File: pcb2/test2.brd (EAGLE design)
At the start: 7 x 6.9 mm, 56 parts, among them IC1 LMV358M, IC2 LMV358M, IC3 STM32F10XCXT6, Q1 8mhz

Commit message: ready to facturing
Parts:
- C-ADCBATT: value (none) -> 100nf
- C-CLK1, C-CLK2: value (none) -> 22pf
- R-ADCBATT2: value 4k7 -> 1k5
- R-ADCLAMP1, R-ADCLAMP2, R-ADCLAMP3, R-ADCPV1, R-ADCPV2, R-ADCPV3, R-ADCUSB1, R-ADCUSB2, R-ADCUSB3: value 4k7 -> 100k
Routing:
- removed copper zone on layer 1, net N$19
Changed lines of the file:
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@@
 <layer number="18" name="Vias" color="2" fill="1" visible="yes" active="yes"/>
 <layer number="19" name="Unrouted" color="6" fill="1" visible="yes" active="yes"/>
-<layer number="20" name="Dimension" color="15" fill="1" visible="yes" active="yes"/>
+<layer number="20" name="Dimension" color="15" fill="1" visible="no" active="yes"/>
 <layer number="21" name="tPlace" color="7" fill="1" visible="yes" active="yes"/>
 <layer number="22" name="bPlace" color="7" fill="1" visible="yes" active="yes"/>
@@
 <text x="77.724" y="15.367" size="1.9304" layer="16" font="vector" ratio="10" rot="MR0">SYSTEM</text>
 <text x="30.861" y="47.879" size="1.9304" layer="16" font="vector" ratio="10" rot="MR0">v2.0</text>
+<wire x1="60.96" y1="45.974" x2="-0.254" y2="45.974" width="0.4064" layer="21"/>
+<wire x1="61.087" y1="47.879" x2="95.885" y2="47.879" width="0.4064" layer="21"/>
+<wire x1="99.949" y1="41.402" x2="76.962" y2="41.402" width="0.4064" layer="21"/>
+<wire x1="74.168" y1="41.529" x2="74.168" y2="31.623" width="0.4064" layer="21"/>
+<wire x1="76.2" y1="36.322" x2="76.2" y2="26.289" width="0.4064" layer="21"/>
+<wire x1="59.182" y1="31.115" x2="43.815" y2="31.115" width="0.4064" layer="21"/>
+<wire x1="39.37" y1="38.1" x2="39.37" y2="27.94" width="0.4064" layer="21"/>
+<wire x1="35.306" y1="39.37" x2="35.306" y2="32.639" width="0.4064" layer="21"/>
+<wire x1="55.499" y1="25.273" x2="22.225" y2="25.273" width="0.4064" layer="21"/>
+<wire x1="51.435" y1="23.241" x2="23.495" y2="23.241" width="0.4064" layer="21"/>
+<wire x1="20.193" y1="26.416" x2="20.193" y2="34.671" width="0.4064" layer="21"/>
+<wire x1="47.117" y1="20.701" x2="18.161" y2="20.701" width="0.4064" layer="21"/>
+<wire x1="44.577" y1="5.207" x2="44.577" y2="15.24" width="0.4064" layer="21"/>
+<wire x1="15.494" y1="23.495" x2="3.556" y2="23.495" width="0.4064" layer="21"/>
+<wire x1="15.24" y1="27.813" x2="4.572" y2="27.813" width="0.4064" layer="21"/>
+<wire x1="15.24" y1="33.02" x2="2.54" y2="33.02" width="0.4064" layer="21"/>
+<wire x1="-3.429" y1="65.024" x2="103.124" y2="65.024" width="0.4064" layer="21"/>
+<wire x1="103.124" y1="65.024" x2="103.124" y2="2.286" width="0.4064" layer="21"/>
+<wire x1="103.124" y1="2.286" x2="-3.429" y2="2.286" width="0.4064" layer="21"/>
+<wire x1="-3.429" y1="2.286" x2="-3.429" y2="65.024" width="0.4064" layer="21"/>
 </plain>
 <attributes>
@@
 <element name="C-USB2" library="resistor" package="E2,5-5" value="220uF" x="80.391" y="34.925"/>
 <element name="IC1" library="linear" package="SO08" value="LMV358M" x="25.908" y="40.386" rot="MR90"/>
-<element name="R-ADCPV2" library="resistor" package="R0805" value="4k7" x="19.812" y="39.624" rot="MR0"/>
-<element name="R-ADCPV1" library="resistor" package="R0805" value="4k7" x="17.018" y="40.513" rot="MR270"/>
-<element name="R-ADCPV3" library="resistor" package="R0805" value="4k7" x="19.812" y="37.719" rot="MR180"/>
+<element name="R-ADCPV2" library="resistor" package="R0805" value="100k" x="19.812" y="39.624" rot="MR0"/>
+<element name="R-ADCPV1" library="resistor" package="R0805" value="100k" x="17.018" y="40.513" rot="MR270"/>
+<element name="R-ADCPV3" library="resistor" package="R0805" value="100k" x="19.812" y="37.719" rot="MR180"/>
 <element name="D-PV1" library="diode" package="DO-214AC" value="" x="17.018" y="46.101" rot="MR90"/>
 <element name="IC2" library="linear" package="SO08" value="LMV358M" x="70.358" y="38.227" rot="MR90"/>
-<element name="R-ADCLAMP2" library="resistor" package="R0805" value="4k7" x="59.055" y="39.751" rot="MR180"/>
-<element name="R-ADCLAMP1" library="resistor" package="R0805" value="4k7" x="55.88" y="40.64" rot="MR90"/>
-<element name="R-ADCLAMP3" library="resistor" package="R0805" value="4k7" x="59.055" y="37.465" rot="MR0"/>
+<element name="R-ADCLAMP2" library="resistor" package="R0805" value="100k" x="59.055" y="39.751" rot="MR180"/>
+<element name="R-ADCLAMP1" library="resistor" package="R0805" value="100k" x="55.88" y="40.64" rot="MR90"/>
+<element name="R-ADCLAMP3" library="resistor" package="R0805" value="100k" x="59.055" y="37.465" rot="MR0"/>
 <element name="D-LAMP1" library="diode" package="DO-214AC" value="" x="55.88" y="46.609" rot="MR90"/>
-<element name="R-ADCUSB1" library="resistor" package="R0805" value="4k7" x="89.535" y="40.132" rot="MR90"/>
-<element name="R-ADCUSB2" library="resistor" package="R0805" value="4k7" x="92.71" y="39.37" rot="MR0"/>
-<element name="R-ADCUSB3" library="resistor" package="R0805" value="4k7" x="92.71" y="37.338" rot="MR180"/>
+<element name="R-ADCUSB1" library="resistor" package="R0805" value="100k" x="89.535" y="40.132" rot="MR90"/>
+<element name="R-ADCUSB2" library="resistor" package="R0805" value="100k" x="92.71" y="39.37" rot="MR0"/>
+<element name="R-ADCUSB3" library="resistor" package="R0805" value="100k" x="92.71" y="37.338" rot="MR180"/>
 <element name="D-USB1" library="diode" package="DO-214AC" value="" x="89.662" y="45.847" rot="MR90"/>
 <element name="LED1" library="led" package="CHIP-LED0805" value="" x="39.624" y="14.351" rot="MR90"/>
@@
 <element name="LED6" library="led" package="CHIP-LED0805" value="" x="39.624" y="24.257" rot="MR90"/>
 <element name="R-ADCBATT1" library="resistor" package="R0805" value="4k7" x="22.987" y="27.432" rot="MR180"/>
-<element name="R-ADCBATT2" library="resistor" package="R0805" value="4k7" x="26.67" y="27.432" rot="MR0"/>
-<element name="C-ADCBATT" library="resistor" package="C0805" value="" x="26.67" y="29.464" rot="MR0"/>
+<element name="R-ADCBATT2" library="resistor" package="R0805" value="1k5" x="26.67" y="27.432" rot="MR0"/>
+<element name="C-ADCBATT" library="resistor" package="C0805" value="100nf" x="26.67" y="29.464" rot="MR0"/>
 <element name="S-NRST" library="switch" package="SKHMPXE010" value="SKHMPSE010" x="11.303" y="23.749" rot="MR0"/>
 <element name="R-NRST" library="resistor" package="R0805" value="4k7" x="17.78" y="23.495" rot="MR90"/>
@@
 <attribute name="OC_FARNELL" value="1667008" x="-31.75" y="-66.929" size="1.778" layer="27" rot="R270" display="off"/>
 </element>
-<element name="C-CLK1" library="resistor" package="C0805" value="" x="14.478" y="12.192" rot="MR270"/>
-<element name="C-CLK2" library="resistor" package="C0805" value="" x="14.605" y="16.129" rot="MR90"/>
+<element name="C-CLK1" library="resistor" package="C0805" value="22pf" x="14.478" y="12.192" rot="MR270"/>
+<element name="C-CLK2" library="resistor" package="C0805" value="22pf" x="14.605" y="16.129" rot="MR90"/>
 <element name="FLASH" library="pinhead" package="1X04" value="" x="37.719" y="10.287" rot="R180"/>
 <element name="X1" library="con-berg" package="PN87520" value="" x="67.056" y="58.547" rot="R180">
@@
 <vertex x="-2.921" y="64.262"/>
 <vertex x="102.362" y="64.262"/>
-<vertex x="102.362" y="2.921"/>
-<vertex x="-2.921" y="2.921"/>
-</polygon>
-</signal>
-<signal name="N$19">
-<polygon width="0.8128" layer="1" isolate="0.8128">
-<vertex x="-2.921" y="64.262"/>
-<vertex x="102.362" y="64.262"/>

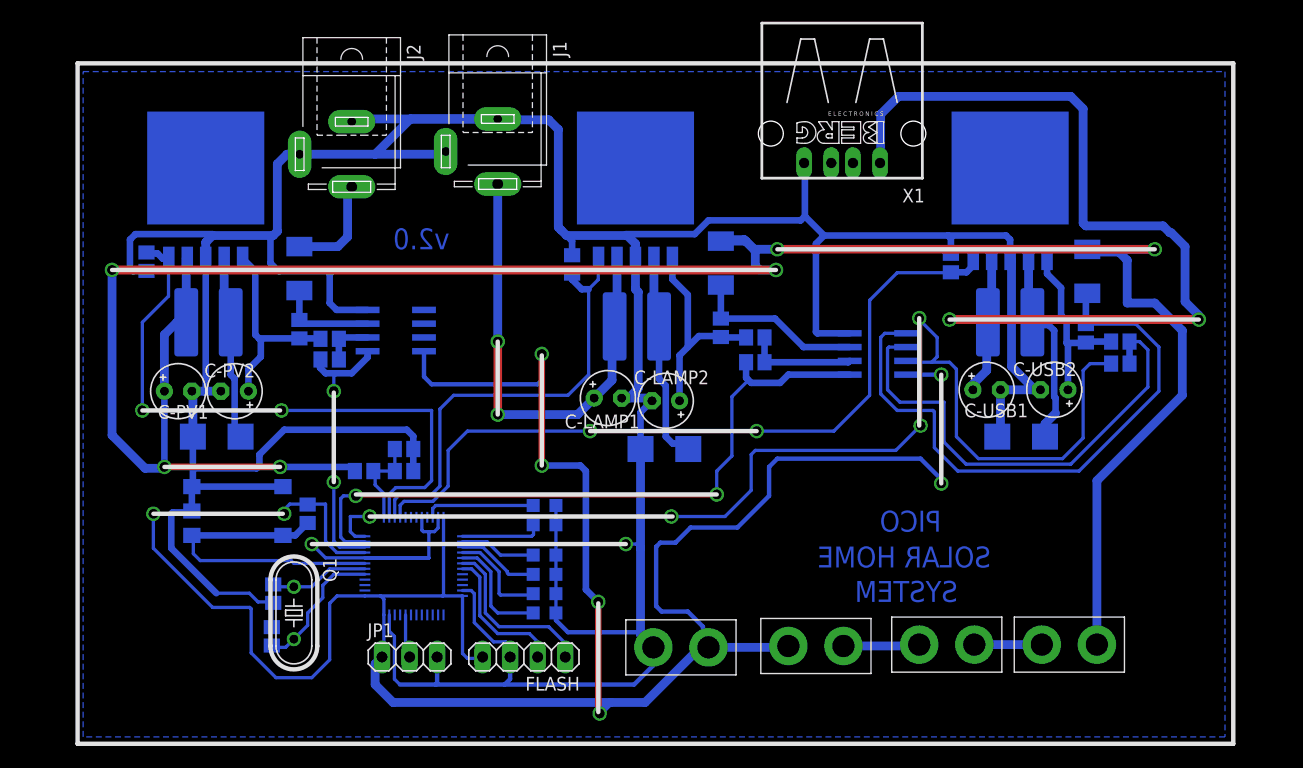
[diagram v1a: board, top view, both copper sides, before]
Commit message: add mount holes
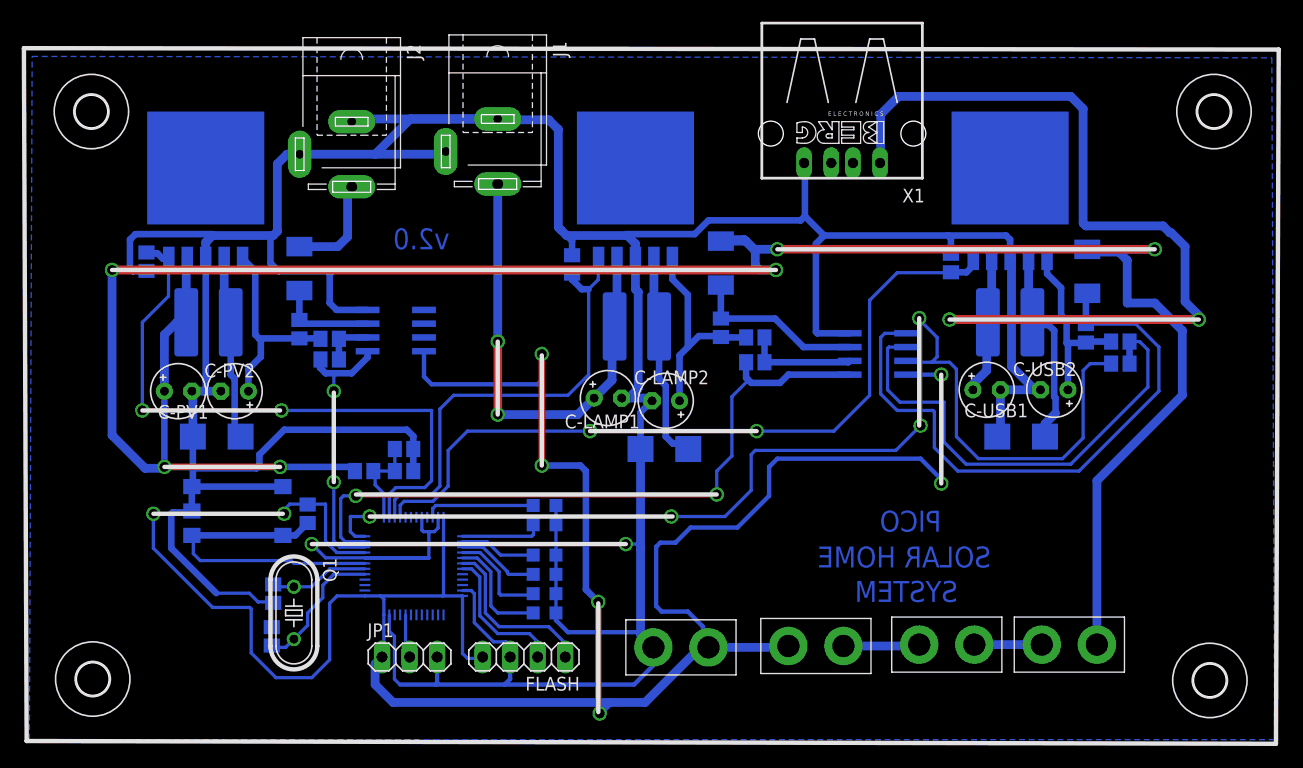
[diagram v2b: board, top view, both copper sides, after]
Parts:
- added H1, H2, H3, H4: MOUNT-HOLE3.0, holes:3,0
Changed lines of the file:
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@@
 <layer number="21" name="tPlace" color="7" fill="1" visible="yes" active="yes"/>
 <layer number="22" name="bPlace" color="7" fill="1" visible="yes" active="yes"/>
-<layer number="23" name="tOrigins" color="15" fill="1" visible="no" active="yes"/>
-<layer number="24" name="bOrigins" color="15" fill="1" visible="no" active="yes"/>
+<layer number="23" name="tOrigins" color="15" fill="1" visible="yes" active="yes"/>
+<layer number="24" name="bOrigins" color="15" fill="1" visible="yes" active="yes"/>
 <layer number="25" name="tNames" color="7" fill="1" visible="no" active="yes"/>
 <layer number="26" name="bNames" color="7" fill="1" visible="no" active="yes"/>
@@
 <wire x1="15.24" y1="27.813" x2="4.572" y2="27.813" width="0.4064" layer="21"/>
 <wire x1="15.24" y1="33.02" x2="2.54" y2="33.02" width="0.4064" layer="21"/>
-<wire x1="-3.429" y1="65.024" x2="103.124" y2="65.024" width="0.4064" layer="21"/>
-<wire x1="103.124" y1="65.024" x2="103.124" y2="2.286" width="0.4064" layer="21"/>
-<wire x1="103.124" y1="2.286" x2="-3.429" y2="2.286" width="0.4064" layer="21"/>
-<wire x1="-3.429" y1="2.286" x2="-3.429" y2="65.024" width="0.4064" layer="21"/>
+<wire x1="-8.382" y1="66.421" x2="107.315" y2="66.294" width="0.4064" layer="21"/>
+<wire x1="107.315" y1="66.294" x2="107.061" y2="2.286" width="0.4064" layer="21"/>
+<wire x1="107.061" y1="2.286" x2="-8.128" y2="2.54" width="0.4064" layer="21"/>
+<wire x1="-8.128" y1="2.54" x2="-8.382" y2="66.421" width="0.4064" layer="21"/>
 </plain>
 <attributes>
@@
 <element name="R-CON-PV" library="resistor" package="R0805" value="4k7" x="2.921" y="46.736" rot="MR90"/>
 <element name="R-CONUSB" library="resistor" package="R0805" value="4k7" x="77.089" y="46.609" rot="MR270"/>
+<element name="H1" library="holes" package="3,0" value="MOUNT-HOLE3.0" x="-2.159" y="60.579"/>
+<element name="H2" library="holes" package="3,0" value="MOUNT-HOLE3.0" x="100.965" y="8.128"/>
+<element name="H3" library="holes" package="3,0" value="MOUNT-HOLE3.0" x="101.346" y="60.579"/>
+<element name="H4" library="holes" package="3,0" value="MOUNT-HOLE3.0" x="-2.032" y="8.255"/>
 </elements>
 <signals>
@@
 <signal name="N$18">
 <polygon width="0.8128" layer="16" isolate="1.016">
-<vertex x="-2.921" y="64.262"/>
-<vertex x="102.362" y="64.262"/>
-<vertex x="102.362" y="2.921"/>
-<vertex x="-2.921" y="2.921"/>
+<vertex x="-7.62" y="65.659"/>
+<vertex x="106.68" y="65.532"/>
+<vertex x="106.934" y="2.667"/>
+<vertex x="-7.874" y="2.667"/>
 </polygon>
 </signal>
